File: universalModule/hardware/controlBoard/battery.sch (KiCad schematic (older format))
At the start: 33 parts, among them Q1 SiA449DJ, Q2 SiA449DJ, Q3 SSM3K72CFS, SW1 START_BUTTON, SW2 STOP_BUTTON, U4 MP2615, U5 BQ29200

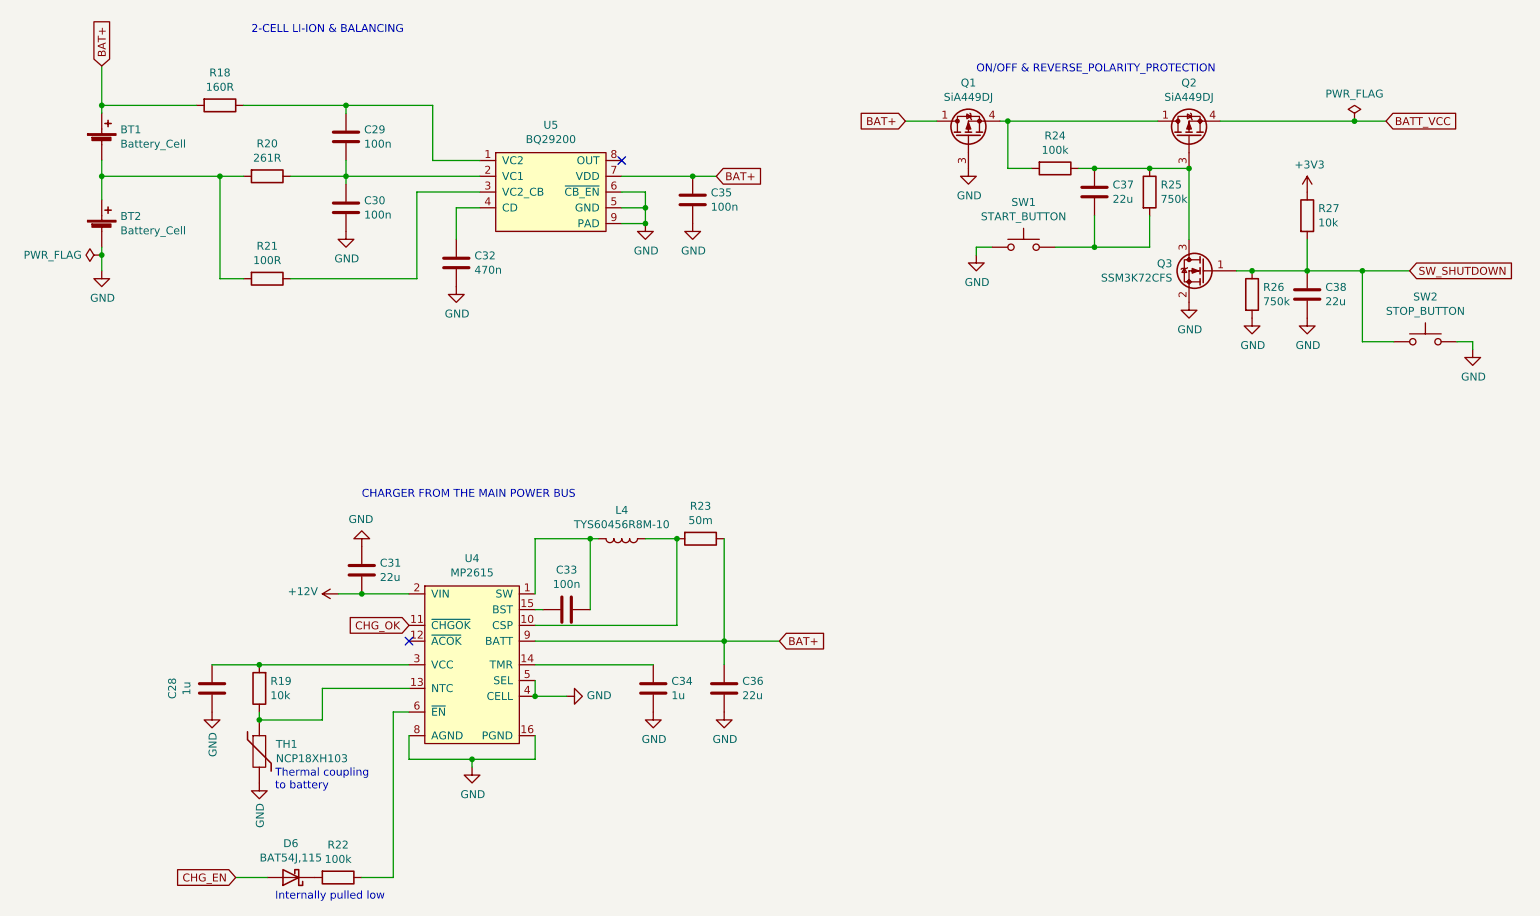
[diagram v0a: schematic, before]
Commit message: universalModule: Route the control boards
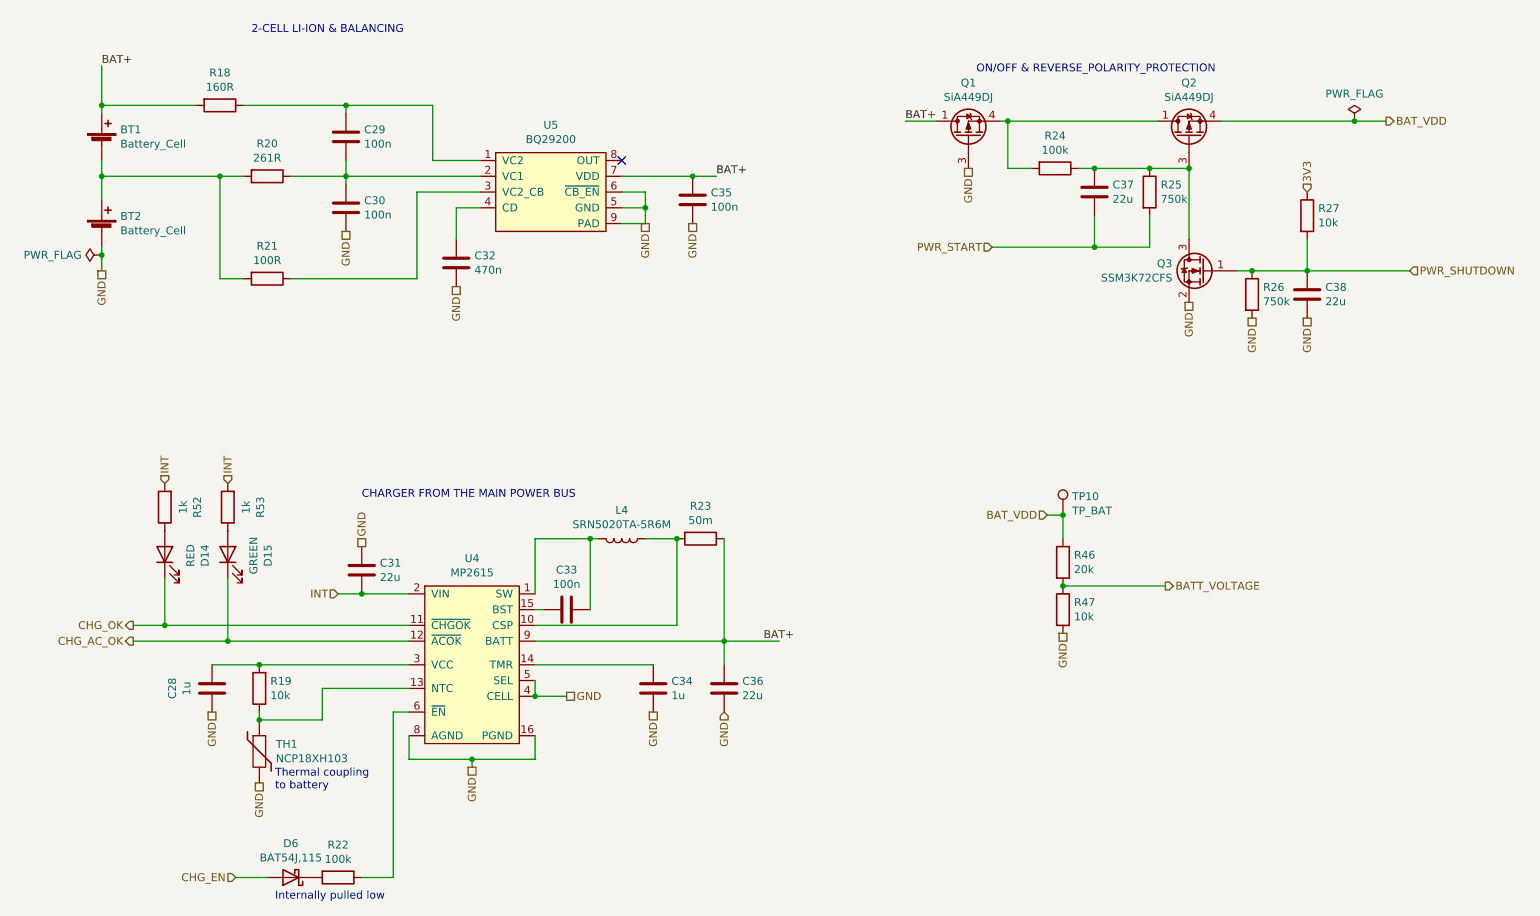
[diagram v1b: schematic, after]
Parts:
- removed SW1: START_BUTTON, rofi:BUTTON_SMT_G_4_3, symbol Switch:SW_Push
- removed SW2: STOP_BUTTON, rofi:BUTTON_SMT_G_4_3, symbol Switch:SW_Push
- added D14: RED, LED_SMD:LED_0603_1608Metric, symbol Device:LED
- added D15: GREEN, LED_SMD:LED_0603_1608Metric, symbol Device:LED
- added R46: 20k, Resistor_SMD:R_0402_1005Metric, symbol Device:R
- added R47: 10k, Resistor_SMD:R_0402_1005Metric, symbol Device:R
- added R52, R53: 1k, Resistor_SMD:R_0402_1005Metric, symbol Device:R
- added TP10: TP_BAT, TestPoint:TestPoint_Pad_D2.0mm, symbol Connector:TestPoint
- BT1, BT2: footprint rofi:KeyStone-18350 -> rofi:BATTERY_18350; #manf 1095P -> (none)
- L4: value TYS60456R8M-10 -> SRN5020TA-5R6M; footprint rofi:TYS6045 -> rofi:SRN5020TA; #manf (none) -> SRN5020TA-5R6M
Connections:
- net CHG_OK: now also D14.1 (K)
- net GND: now also R47.2
- net CHG_AC_OK: now reaches U4.12 (~ACOK)
- net CHG_AC_OK: now also D15.1 (K)
- net PWR_START: now reaches C37.2, R25.2
- net +12V renamed INT
- net INT: now also R52.2, R53.2
- net +3V3 renamed 3V3
- net BATT_VCC renamed BAT_VDD
- net BAT_VDD: now also R46.1, TP10.1
- net SW_SHUTDOWN renamed PWR_SHUTDOWN
- new net: D14.2 (A), R52.1
- new net: D15.2 (A), R53.1
- new net BATT_VOLTAGE: R46.2, R47.1
- no-connect marks 2 -> 1

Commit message: UniversalModule: Start version 2
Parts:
- removed C28, C34: 1u, Capacitor_SMD:C_0402_1005Metric, symbol Device:C
- removed C29, C30, C33, C35: 100n, Capacitor_SMD:C_0402_1005Metric, symbol Device:C
- removed C31, C36: 22u, Capacitor_SMD:C_0805_2012Metric, symbol Device:C
- removed C32: 470n, Capacitor_SMD:C_0402_1005Metric, symbol Device:C
- removed D15: GREEN, LED_SMD:LED_0603_1608Metric, symbol Device:LED
- removed D6: BAT54J,115, Diode_SMD:D_SOD-323, symbol Device:D_Schottky
- removed L4: SRN5020TA-5R6M, rofi:SRN5020TA, symbol Device:L
- removed Q1, Q2: SiA449DJ, Package_TO_SOT_SMD:Vishay_PowerPAK_SC70-6L_Single, symbol Transistor_FET:SiA449DJ
- removed Q3: SSM3K72CFS, Package_TO_SOT_SMD:SOT-416, symbol Device:Q_NMOS_GSD
- removed R18: 160R, Resistor_SMD:R_0402_1005Metric, symbol Device:R
- removed R19, R47: 10k, Resistor_SMD:R_0402_1005Metric, symbol Device:R
- removed R20: 261R, Resistor_SMD:R_0402_1005Metric, symbol Device:R
- removed R21: 100R, Resistor_SMD:R_0402_1005Metric, symbol Device:R
- removed R22: 100k, Resistor_SMD:R_0402_1005Metric, symbol Device:R
- removed R23: 50m, Resistor_SMD:R_1206_3216Metric, symbol Device:R
- removed R46: 20k, Resistor_SMD:R_0402_1005Metric, symbol Device:R
- removed R52, R53: 1k, Resistor_SMD:R_0402_1005Metric, symbol Device:R
- removed TH1: NCP18XH103, Resistor_SMD:R_0603_1608Metric, symbol Device:Thermistor
- removed TP10: TP_BAT, TestPoint:TestPoint_Pad_D2.0mm, symbol Connector:TestPoint
- removed U4: MP2615, rofi:QFN-16, symbol rofi:MP2615
- removed U5: BQ29200, Package_SON:Texas_S-PVSON-N8, symbol rofi:BQ29200
- added C? (x3): 100n, Capacitor_SMD:C_0402_1005Metric, symbol Device:C
- added C? (x2): 10u, Capacitor_SMD:C_0805_2012Metric, symbol Device:C
- added C? (x4): 22u, Capacitor_SMD:C_0805_2012Metric, symbol Device:C
- added D?: SS54, Diode_SMD:D_SMA, symbol Device:D_Schottky
- added L?: 22u, rofi:SLO0630H, symbol Device:L
- added Q? (x2): NCE20P45Q, rofi:DFN3.3X3.3-EP, symbol Device:Q_PMOS_SGD
- added Q?: 2N7002, Package_TO_SOT_SMD:SOT-23, symbol Transistor_FET:2N7002
- added R?: 75m, Resistor_SMD:R_1206_3216Metric, symbol Device:R
- added R?: 0R, Resistor_SMD:R_0402_1005Metric, symbol Device:R
- added R?: 470R, symbol Device:R
- added U?: TP5100, Package_DFN_QFN:QFN-16-1EP_4x4mm_P0.65mm_EP2.1x2.1mm, symbol rofi:TP5100
- C37, C38: LCSC (none) -> C45783
- D14: LCSC (none) -> C2286
- R24: LCSC (none) -> C25741
- R25, R26: value 750k -> 100k; LCSC (none) -> C25741
- R27: LCSC (none) -> C25744
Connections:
- net 3V3: now also R?.2
- net BAT+: now also C?.1, C?.1, C?.1, D?.2 (A), Q?.3 (D), R?.1, U?.9 (BAT)
- net BAT_VDD: now also Q?.3 (D)
- net CHG_EN: now also U?.13 (CELL_SELECT)
- net CHG_OK: now also U?.15 (~CHRG)
- net GND: now also C?.2, C?.2, C?.2, C?.2, C?.2, C?.2, C?.2, C?.2, C?.2, Q?.2 (G), Q?.2 (S), R?.2, U?.11 (TS), U?.17 (PAD), U?.7 (VSS)
- net INT: now also C?.1, C?.1, C?.1, U?.1 (VIN), U?.16 (VIN), U?.4 (VIN), U?.5 (VIN)
- net PWR_SHUTDOWN: now also Q?.1 (G)
- net at D14.2 (A): now also R?.1
- net at R24.2: now also Q?.1 (S), Q?.1 (S)
- net at C37.1, R24.1, R25.1: now also Q?.2 (G), Q?.3 (D)
- new net: C?.1, U?.10 (VREG)
- new net: R?.1, U?.12 (RTRICK)
- new net: L?.1, U?.2 (LX), U?.3 (LX)
- new net: C?.1, C?.1, D?.1 (K), L?.2, R?.2, U?.8 (VS)
- no-connect marks 1 -> 2
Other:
- note added: "Note that cell select:\n- LOW: shutdown\n- HIGH: 2 cells\n- FLOATING: 1 cell"
- note removed: "2-CELL LI-ION & BALANCING"
- note removed: "Internally pulled low"
- note removed: "Thermal coupling\nto battery"
- moved on the sheet: BT1, BT2, C37, D14, R24, R25
